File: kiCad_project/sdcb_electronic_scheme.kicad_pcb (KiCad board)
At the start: 2 copper layers, 144.8 x 99.1 mm, 70 parts, among them CON1 SD_Card, J1 POWER_12V, J10 BUTTON_RIGHT_TURN, J11 DB9, J2 Arduino_Nano_Header, J3 REAL_TIME_CLOCK, J4 LEFT_TURN_GYRO, J5 RIGHT_TURN_GYRO, J6 POWER_12V, J7 MOTOR, J8 BUTTON_ALL_DOWN_READ, J9 BUTTON_LEFT_TURN, Q1 BC817-40, Q2 BC817-40, U1 74HC595

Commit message: PCB v1
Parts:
- removed R18: 220 Ohm, Resistors_ThroughHole:Resistor_Horizontal_RM10mm
- added D16: D_Schottky, Diodes_ThroughHole:Diode_DO-41_SOD81_Horizontal_RM10, F.Cu at (71.1, 70.5)
- added D25: D_Schottky, Diodes_ThroughHole:Diode_DO-41_SOD81_Horizontal_RM10, F.Cu at (71.1, 64.1)
- added D26: D_Schottky, Diodes_ThroughHole:Diode_DO-41_SOD81_Horizontal_RM10, F.Cu at (71.1, 61.0)
- added D27: D_Schottky, Diodes_ThroughHole:Diode_DO-41_SOD81_Horizontal_RM10, F.Cu at (71.1, 57.8)
- added D28: D_Schottky, Diodes_ThroughHole:Diode_DO-41_SOD81_Horizontal_RM10, F.Cu at (72.4, 123.2)
- added D29: D_Schottky, Diodes_ThroughHole:Diode_DO-41_SOD81_Horizontal_RM10, F.Cu at (72.4, 119.4)
- added D30: D_Schottky, Diodes_ThroughHole:Diode_DO-41_SOD81_Horizontal_RM10, F.Cu at (72.4, 115.6)
- added D31: D_Schottky, Diodes_ThroughHole:Diode_DO-41_SOD81_Horizontal_RM10, F.Cu at (72.4, 111.8)
- added D32: D_Schottky, Diodes_ThroughHole:Diode_DO-41_SOD81_Horizontal_RM10, F.Cu at (72.4, 108.0)
- added D33: D_Schottky, Diodes_ThroughHole:Diode_DO-41_SOD81_Horizontal_RM10, F.Cu at (72.4, 100.3)
- added D34: D_Schottky, Diodes_ThroughHole:Diode_DO-41_SOD81_Horizontal_RM10, F.Cu at (256.5, -4.45)
- added D35: D_Schottky, Diodes_ThroughHole:Diode_DO-41_SOD81_Horizontal_RM10, F.Cu at (151.1, 161.3)
- added D36: D_Schottky, Diodes_ThroughHole:Diode_DO-41_SOD81_Horizontal_RM10, F.Cu at (240.7, -22.2)
- added J12: RELAY_CONTROL, Pin_Headers:Pin_Header_Straight_1x02, F.Cu at (388.6, 63.8)
- added J13: 220V, Connect:AK300-2, F.Cu at (160.0, 55.9)
- added J14: 30V MOTOR, Connect:AK300-2, F.Cu at (146.1, 55.9)
- added Q3: BC817-40, Housings_TO-92:TO-92_Molded_Wide_Oval, F.Cu at (330.7, 128.9)
- added RL3: FINDER-36.11.4001, sun_hold:sun_hold_scb1m1240, F.Cu at (236.9, -3.81)
- added U2: 74HC595, Housings_DIP:DIP-16_W7.62mm_LongPads, F.Cu at (87.6, 79.4)
- added U3: 74HC595, Housings_DIP:DIP-16_W7.62mm_LongPads, F.Cu at (87.6, 55.9)
- added U4: 74HC595, Housings_DIP:DIP-16_W7.62mm_LongPads, F.Cu at (87.6, 104.8)
- added U5: LTV-817, Housings_DIP:DIP-4_W7.62mm, F.Cu at (338.8, 116.3)
- added U6: LTV-817, Housings_DIP:DIP-4_W7.62mm_LongPads, F.Cu at (288.4, 121.9)
- added U7: LTV-817, Housings_DIP:DIP-4_W7.62mm_LongPads, F.Cu at (251.4, 148.6)
- added X1: Buzzer, Buzzer_Beeper_RevA_25Oct2010:MagneticBuzzer_ProSignal_ABT-410-RC_RevA_25Oct2010, F.Cu at (-21.0, 121.3)
- C2: value 2200 uF -> 2200uF 25V
- D10, D12, D14, D15, D8: value 5.1V 1.3W -> D_Schottky; footprint Discret:D3 -> Diodes_ThroughHole:Diode_DO-41_SOD81_Horizontal_RM10
- D17: value LED -> D_Schottky; footprint LEDs:LED-3MM -> Diodes_ThroughHole:Diode_DO-41_SOD81_Horizontal_RM10
- D2, D3, D4: value D -> 100V 2A
- J1, J7: footprint Pin_Headers:Pin_Header_Straight_2x01 -> Connect:AK300-2
- J10: value BUTTON_RIGHT_TURN -> B_RIGHT_T
- J11: footprint Connect:DB9MD -> Connect:DB9FC
- J6: value POWER_12V -> POWER_MOTOR; footprint Pin_Headers:Pin_Header_Straight_2x01 -> Connect:AK300-2
- J8: value BUTTON_ALL_DOWN_READ -> DB15; footprint Pin_Headers:Pin_Header_Straight_2x01 -> Connect:DB15FC
- J9: value BUTTON_LEFT_TURN -> B_LEFT_T
- Q1, Q2: footprint trans:TO-220_Bipolar-BCE_Vertical_LargePads -> Housings_TO-92:TO-92_Molded_Wide_Oval
- R11, R12, R16: value 100 Ohm -> 1k
- R13, R14, R15: value R -> 1k
- R19: value R -> 220Ohm
- R7, R8: value 1k -> 10k
- moved R5 306.4 mm to (385.4, 52.8), turned to 0 degrees
- moved R14 296.7 mm to (363.5, 88.0), turned to 0 degrees
- moved CON1 291.0 mm to (374.6, 195.6), turned to 0 degrees
- moved R13 279.5 mm to (348.5, 105.2), turned to 0 degrees
- moved R1 277.3 mm to (363.5, 78.6), turned to 0 degrees
- moved R6 268.3 mm to (351.0, 86.0), turned to 0 degrees
- moved R10 267.4 mm to (363.5, 69.2), turned to 0 degrees
- moved R4 251.2 mm to (336.0, 105.2), turned to 0 degrees
- moved Q2 243.8 mm to (386.6, 74.5), turned to 0 degrees
- moved R16 233.0 mm to (304.5, 149.4), turned to 0 degrees
- moved C3 226.4 mm to (299.4, 158.8), turned to 0 degrees
- moved R3 224.8 mm to (307.6, 128.6), turned to 0 degrees
- moved R15 220.9 mm to (292.0, 158.8), turned to 0 degrees
- moved Q1 215.9 mm to (361.1, 100.6), turned to 0 degrees
- moved J3 215.7 mm to (335.0, 54.4)
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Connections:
- D10 pad 2: GND -> Net-(D10-Pad2)
- D12 pad 2: GND -> Net-(D12-Pad2)
- D14 pad 2: GND -> Net-(D14-Pad2)
- D15 pad 2: GND -> Net-(D15-Pad2)
- D17 pad 1: GND -> Net-(D17-Pad1)
- D8 pad 2: GND -> Net-(D8-Pad2)
- F1 pad 1: +12V -> Net-(D3-Pad1)
- F1 pad 2: Net-(D3-Pad1) -> +12V
- J1 pad 1: Net-(D1-Pad1) -> Net-(D2-Pad1)
- J1 pad 2: Net-(D2-Pad1) -> Net-(D1-Pad1)
- J10 pad 1: Net-(J10-Pad1) -> Net-(D32-Pad1)
- J10 pad 2: GND -> Net-(J10-Pad2)
- J11 pad 2: Net-(J11-Pad2) -> Net-(D29-Pad1)
- J11 pad 3: Net-(J11-Pad3) -> Net-(D30-Pad1)
- J11 pad 4: Net-(J11-Pad4) -> Net-(D31-Pad1)
- J11 pad 6: GND -> Net-(J10-Pad2)
- J11 pad 7: GND -> Net-(J10-Pad2)
- J11 pad 8: GND -> Net-(J10-Pad2)
- J11 pad 9: GND -> Net-(J10-Pad2)
- J2 pad 16: Net-(D15-Pad1) -> Net-(J2-Pad16)
- J2 pad 19: Net-(D13-Pad1) -> Net-(J2-Pad19)
- J2 pad 27: +5V -> VCC
- J2 pad 5: Net-(D8-Pad1) -> Net-(J2-Pad5)
- J2 pad 6: Net-(D10-Pad1) -> Net-(J10-Pad2)
- J2 pad 7: Net-(D12-Pad1) -> Net-(C3-Pad2)
- J2 pad 8: Net-(D14-Pad1) -> Net-(J2-Pad8)
- J2 pad 9: Net-(C3-Pad2) -> Net-(J2-Pad9)
- J3 pad 4: +5V -> VCC
- J4 pad 1: +5V -> VCC
- J5 pad 1: +5V -> VCC
- J6 pad 1: Net-(F2-Pad2) -> Net-(F2-Pad1)
- J8 pad 1: Net-(J8-Pad1) -> Net-(D6-Pad1)
- J8 pad 2: Net-(J8-Pad2) -> Net-(D7-Pad1)
- J9 pad 1: Net-(J9-Pad1) -> Net-(D33-Pad1)
- J9 pad 2: GND -> Net-(J10-Pad2)
- Q1 pad 2: Net-(D6-Pad2) -> GND
- Q1 pad 3: GND -> Net-(D34-Pad2)
- Q2 pad 2: Net-(D7-Pad2) -> GND
- Q2 pad 3: GND -> Net-(D35-Pad2)
- R11 pad 1: Net-(J9-Pad1) -> Net-(R11-Pad1)
- R11 pad 2: Net-(D15-Pad1) -> GND
- R12 pad 1: Net-(J10-Pad1) -> VCC
- R12 pad 2: Net-(D13-Pad1) -> Net-(R12-Pad2)
- R13 pad 1: Net-(D8-Pad1) -> Net-(R13-Pad1)
- R13 pad 2: Net-(J11-Pad2) -> GND
- R14 pad 1: Net-(D10-Pad1) -> Net-(R14-Pad1)
- R14 pad 2: Net-(J11-Pad3) -> GND
- R15 pad 1: Net-(D12-Pad1) -> VCC
- R15 pad 2: Net-(J11-Pad4) -> Net-(R15-Pad2)
- R16 pad 1: Net-(D14-Pad1) -> VCC
- R16 pad 2: Net-(J11-Pad5) -> Net-(R16-Pad2)
- R7 pad 1: Net-(Q1-Pad1) -> Net-(R7-Pad1)
- R7 pad 2: Net-(J2-Pad1) -> GND
- R8 pad 1: Net-(J2-Pad2) -> Net-(R8-Pad1)
- R8 pad 2: Net-(Q2-Pad1) -> Net-(R8-Pad2)
- RL1 pad 12: Net-(Current1-Pad2) -> GND
- RL1 pad 14: Net-(F2-Pad1) -> Net-(F2-Pad2)
- RL1 pad A1: Net-(D6-Pad1) -> Net-(D34-Pad2)
- RL1 pad A2: Net-(Current1-Pad2) -> VCC
- RL2 pad 11: Net-(J7-Pad2) -> Net-(J14-Pad2)
- RL2 pad 14: Net-(F2-Pad1) -> Net-(J13-Pad1)
- RL2 pad A1: Net-(D7-Pad1) -> Net-(D35-Pad2)
- RL2 pad A2: GND -> VCC
- U1 pad 10: GND -> VCC
- U1 pad 11: Net-(J2-Pad10) -> Net-(J2-Pad8)
- U1 pad 13: +5V -> GND
- U1 pad 14: Net-(J2-Pad11) -> Net-(J2-Pad9)
- U1 pad 16: +5V -> VCC
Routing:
- net VCC: track 0.00 -> 94.0 mm
- net GND: track 0.00 -> 82.6 mm
- net Net-(D27-Pad1): track 0.00 -> 45.3 mm
- net Net-(D3-Pad1): track 0.00 -> 39.2 mm
- net Net-(D26-Pad1): track 0.00 -> 37.1 mm
- net Net-(D2-Pad1): track 0.00 -> 35.7 mm
- net +12V: track 0.00 -> 31.0 mm
- net Net-(D25-Pad1): track 0.00 -> 29.0 mm
- net Net-(R25-Pad1): track 0.00 -> 22.0 mm
- net Net-(D1-Pad1): track 0.00 -> 20.9 mm
- net Net-(D17-Pad1): track 0.00 -> 14.0 mm
- net Net-(D33-Pad2): track 0.00 -> 10.2 mm
- net Net-(R24-Pad1): track 0.00 -> 9.72 mm
- net Net-(U1-Pad7): track 0.00 -> 8.59 mm
- net Net-(D14-Pad2): track 0.00 -> 8.46 mm
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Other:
- net class Default: clearance 0.2 -> 0.4; trace_width 0.25 -> 0.5; via_dia 0.6 -> 1.5; via_drill 0.4 -> 0.7
- rule trace_clearance: 0.2 -> 0.4
- rule trace_min: 0.2 -> 0.5
- rule via_min_drill: 0.3 -> 0.7
- rule via_min_size: 0.4 -> 1.5

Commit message: PCB v2
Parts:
- added C4: 0.1 uF, Capacitors_ThroughHole:C_Disc_D6_P5, F.Cu at (98.0, 66.5)
- U6, U7: footprint Housings_DIP:DIP-4_W7.62mm_LongPads -> Housings_DIP:DIP-4_W7.62mm
- moved J7 272.9 mm to (402.0, 96.4), turned to 270 degrees
- moved RL2 252.7 mm to (377.7, 75.9), turned to 180 degrees
- moved J14 251.5 mm to (397.0, 72.4), turned to 90 degrees
- moved C3 239.5 mm to (60.3, 172.1), turned to 270 degrees
- moved J13 238.7 mm to (397.0, 84.1), turned to 90 degrees
- moved D35 237.5 mm to (371.9, 73.7), turned to 0 degrees
- moved RL1 221.6 mm to (382.9, 107.2), turned to 180 degrees
- moved D36 217.9 mm to (387.9, 138.4)
- moved RL3 202.0 mm to (382.9, 135.8)
- moved J6 200.7 mm to (363.5, 128.8), turned to 90 degrees
- moved R5 200.3 mm to (271.3, 217.4)
- moved R1 187.5 mm to (260.9, 235.5), turned to 270 degrees
- moved D34 163.2 mm to (377.7, 104.9)
- moved F2 157.2 mm to (359.9, 114.6)
- moved R6 147.3 mm to (284.5, 217.4)
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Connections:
- Current1 pad 1: GND -> Net-(Current1-Pad1)
- J6 pad 1: Net-(F2-Pad1) -> Net-(Current1-Pad2)
- J6 pad 2: GND -> Net-(F2-Pad1)
- R10 pad 2: GND -> Net-(Current1-Pad1)
- RL1 pad 12: GND -> Net-(Current1-Pad1)
- RL3 pad 12: Net-(Current1-Pad2) -> Net-(Current1-Pad1)
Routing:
- net GND: track 82.6 -> 158.2 mm
- net VCC: track 94.0 -> 153.0 mm
- net Net-(J7-Pad2): track 0.00 -> 53.8 mm
- net Net-(D35-Pad2): track 0.00 -> 38.1 mm
- net Net-(CON1-Pad5): track 0.00 -> 36.0 mm
- net Net-(D34-Pad2): track 0.00 -> 31.0 mm
- net Net-(F2-Pad2): track 0.00 -> 30.2 mm
- net Net-(Current1-Pad1): track 0.00 -> 29.2 mm
- net Net-(D36-Pad2): track 0.00 -> 26.1 mm
- net Net-(F2-Pad1): track 0.00 -> 20.6 mm
- net Net-(J7-Pad1): track 0.00 -> 20.5 mm
- net Net-(J13-Pad1): track 0.00 -> 19.9 mm
- net Net-(J14-Pad2): track 0.00 -> 19.8 mm
- net Net-(CON1-Pad2): track 0.00 -> 12.8 mm
- net Net-(Q2-Pad1): track 0.00 -> 11.5 mm
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
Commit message: 39 left39 left39 left
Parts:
- added 0R1: 0R, Resistors_ThroughHole:Resistor_Horizontal_RM10mm, F.Cu at (106.2, 86.9)
- added 0R2: 0R, Resistors_ThroughHole:Resistor_Horizontal_RM10mm, F.Cu at (103.6, 114.8)
- added 0R3: 0R, Resistors_ThroughHole:Resistor_Horizontal_RM10mm, F.Cu at (106.2, 111.5)
- added 0R4: 0R, Resistors_ThroughHole:Resistor_Horizontal_RM10mm, F.Cu at (100.6, 86.9)
- added R17: 0R, Resistors_ThroughHole:Resistor_Horizontal_RM15mm, F.Cu at (105.2, 101.1)
- CON1: footprint Connect:SD_Card_Receptacle -> Attend_SD_card_socket:SD_Attend
- Current1: footprint Resistors_ThroughHole:Resistor_Ceramic_Horizontal_L50mm-W14mm-H13mm-p60mm -> Resistor10W_vertical:Resistor_Horizontal_RM15mm
- D32, D33: footprint Diodes_ThroughHole:Diode_DO-41_SOD81_Horizontal_RM10 -> Diode_Smaller:Diode_DO-41_SOD81_Horizontal_RM10_SMALLER
- Q3: footprint Housings_TO-92:TO-92_Molded_Wide_Oval -> Housings_TO-92:TO-92_Inline_Wide
- R1: footprint Resistors_ThroughHole:Resistor_Horizontal_RM10mm -> Resistors_ThroughHole:Resistor_Horizontal_RM15mm
- R8: value 10k -> 1k
- RL2: footprint sun_hold:sun_hold_scb1m1240 -> sun_hold_ras0515:Relay_RAS-0515
- X1: footprint Buzzer_Beeper_RevA_25Oct2010:MagneticBuzzer_ProSignal_ABT-410-RC_RevA_25Oct2010 -> Buzzer_Beeper_RevA_25Oct2010:MagneticBuzzer_ProSignal_ABI-010-RC_RevA_25Oct2010
- moved J14 286.7 mm to (123.2, 157.4), turned to 0 degrees
- moved J13 283.5 mm to (123.2, 157.4), turned to 0 degrees
- moved RL2 276.9 mm to (113.7, 159.4), turned to 0 degrees
- moved D36 251.7 mm to (136.9, 118.9), turned to 90 degrees
- moved D35 250.0 mm to (122.2, 60.2), turned to 90 degrees
- moved D18 248.6 mm to (247.4, 68.6), turned to 270 degrees
- moved U6 245.9 mm to (111.5, 52.8)
- moved Q2 245.8 mm to (116.1, 53.1)
- moved R13 245.8 mm to (113.5, 50.0)
- moved R15 245.8 mm to (113.5, 63.8)
- moved R14 245.1 mm to (120.0, 110.5), turned to 270 degrees
- moved RL3 244.3 mm to (139.6, 113.9), turned to 270 degrees
- moved R16 243.8 mm to (123.2, 110.5), turned to 90 degrees
- moved D19 243.6 mm to (247.4, 74.7), turned to 270 degrees
- moved D20 239.1 mm to (247.4, 80.3), turned to 270 degrees
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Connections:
- C4 pad 1: Net-(C4-Pad1) -> Net-(0R2-Pad2)
- J2 pad 1: Net-(J2-Pad1) -> Net-(0R4-Pad1)
- J2 pad 16: Net-(J2-Pad16) -> Net-(C3-Pad2)
- J2 pad 2: Net-(J2-Pad2) -> Net-(0R2-Pad2)
- J2 pad 5: Net-(C4-Pad1) -> Net-(0R3-Pad2)
- J2 pad 6: Net-(J10-Pad2) -> Net-(D13-Pad1)
- J2 pad 7: Net-(C3-Pad2) -> Net-(J2-Pad7)
- R7 pad 1: Net-(R7-Pad1) -> Net-(R17-Pad1)
- R8 pad 1: Net-(R8-Pad1) -> Net-(R17-Pad1)
- R8 pad 2: Net-(R8-Pad2) -> Net-(D13-Pad1)
- U2 pad 11: Net-(J2-Pad10) -> Net-(0R4-Pad1)
- U2 pad 12: Net-(C4-Pad1) -> Net-(0R2-Pad2)
- U2 pad 14: Net-(J2-Pad11) -> Net-(U2-Pad14)
- U3 pad 11: Net-(J2-Pad10) -> Net-(0R4-Pad2)
- U3 pad 12: Net-(C4-Pad1) -> Net-(0R2-Pad2)
- U3 pad 14: Net-(U2-Pad9) -> Net-(0R1-Pad1)
- U3 pad 9: Net-(U3-Pad9) -> Net-(U2-Pad14)
- U4 pad 11: Net-(J2-Pad10) -> Net-(0R4-Pad1)
- U4 pad 12: Net-(C4-Pad1) -> Net-(0R2-Pad1)
- U4 pad 14: Net-(U3-Pad9) -> Net-(0R3-Pad1)
- U5 pad 1: Net-(J2-Pad2) -> Net-(J2-Pad11)
- U6 pad 1: Net-(J2-Pad16) -> Net-(J2-Pad7)
- U7 pad 1: Net-(J2-Pad1) -> Net-(J2-Pad10)
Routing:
- net Net-(CON1-Pad7): track 0.00 -> 97.7 mm
- net Net-(J10-Pad2): track 0.00 -> 89.2 mm
- net GND: track 158.2 -> 238.2 mm
- net Net-(0R2-Pad2): track 0.00 -> 79.7 mm
- net Net-(J2-Pad11): track 0.00 -> 78.4 mm
- net Net-(J2-Pad7): track 0.00 -> 53.7 mm
- net Net-(0R4-Pad1): track 0.00 -> 53.5 mm
- net +3V3: track 0.00 -> 44.5 mm
- net Net-(0R1-Pad2): track 0.00 -> 37.9 mm
- net Net-(J2-Pad24): track 0.00 -> 33.8 mm
- net Net-(J2-Pad23): track 0.00 -> 33.8 mm
- net Net-(0R1-Pad1): track 0.00 -> 29.6 mm
- net Net-(0R3-Pad2): track 0.00 -> 28.4 mm
- net Net-(J2-Pad12): track 0.00 -> 26.6 mm
- net Net-(CON1-Pad1): track 8.80 -> 34.5 mm
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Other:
- board text added: "pakeisti sd kortelę, pridėt RTC virš jos it pakeisti pinus pagal RTC ir gyro. ir tada tranzo kojas vienoj eilėj padaryti"

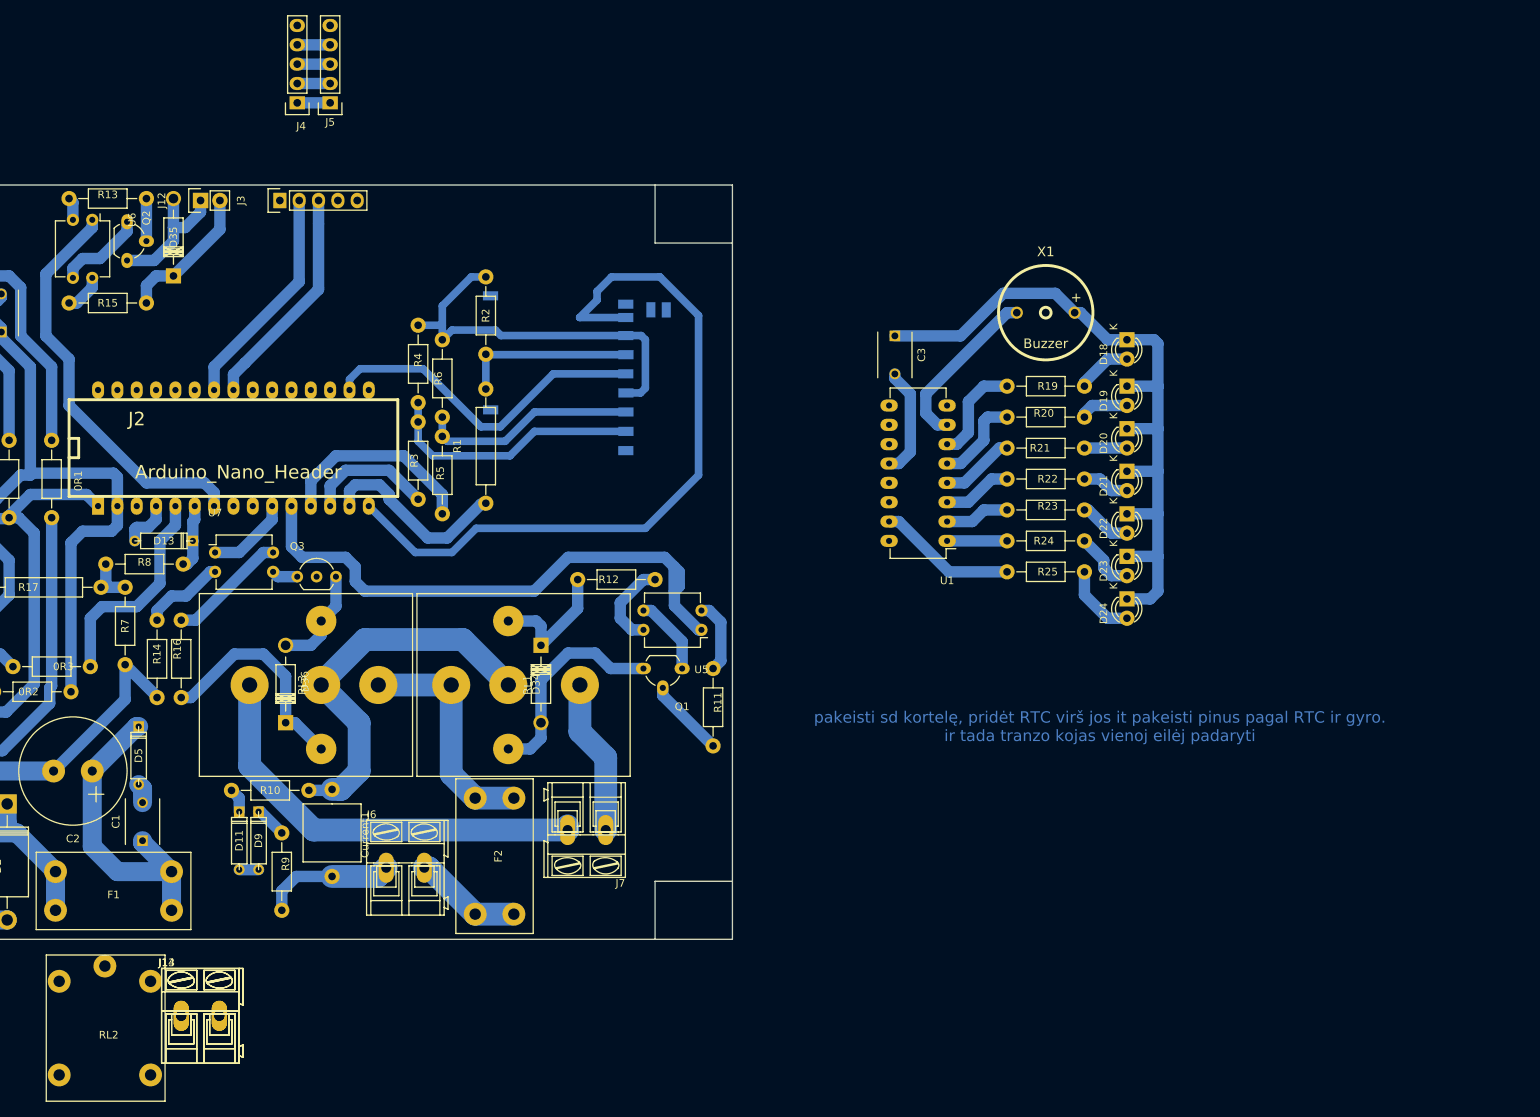
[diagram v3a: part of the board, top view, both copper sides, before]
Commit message: LEDs separated
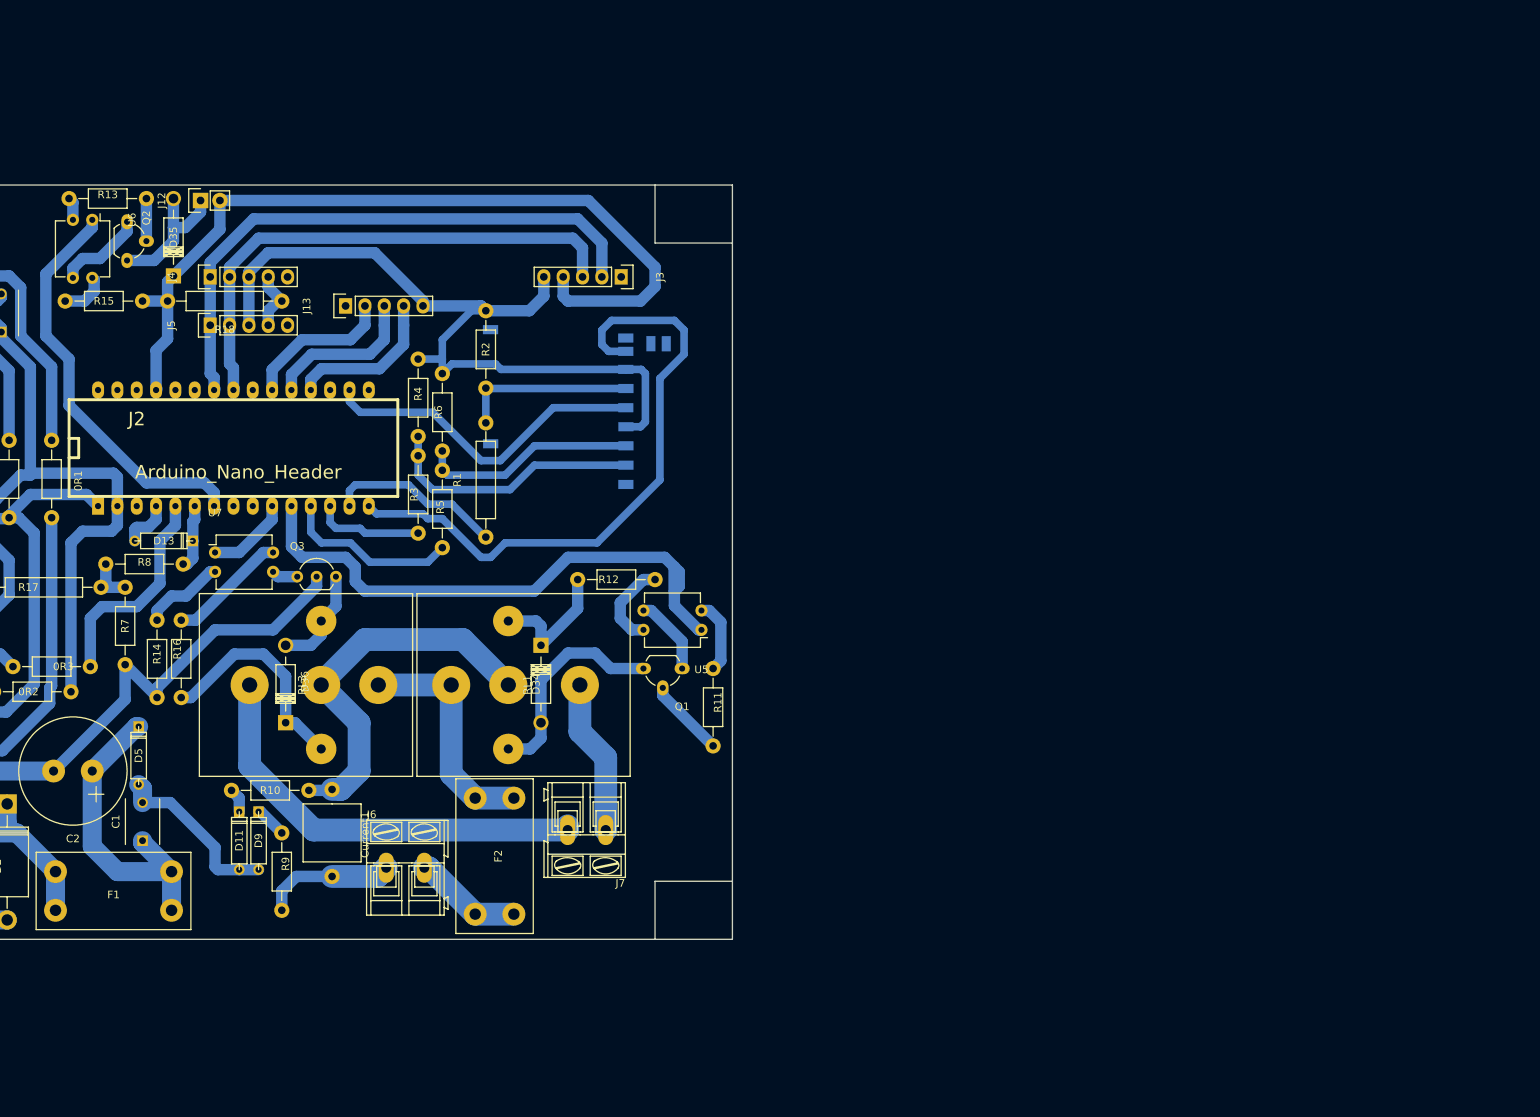
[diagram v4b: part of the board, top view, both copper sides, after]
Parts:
- removed C3: 0.1 uF, Capacitors_ThroughHole:C_Disc_D6_P5
- removed D18, D19, D20, D21, D22, D23, D24: LED, LEDs:LED-3MM
- removed J14: 30V MOTOR, Connect:AK300-2
- removed R19: 220Ohm, Resistors_ThroughHole:Resistor_Horizontal_RM10mm
- removed R20, R21, R22, R23, R24, R25: R, Resistors_ThroughHole:Resistor_Horizontal_RM10mm
- removed RL2: FINDER-36.11.4001, sun_hold_ras0515:Relay_RAS-0515
- removed U1: 74HC595, Housings_DIP:DIP-16_W7.62mm_LongPads
- removed X1: Buzzer, Buzzer_Beeper_RevA_25Oct2010:MagneticBuzzer_ProSignal_ABI-010-RC_RevA_25Oct2010
- added R18: 0R, Resistors_ThroughHole:Resistor_Horizontal_RM15mm, F.Cu at (128.9, 63.5)
- J13: value 220V -> HEADER_5; footprint Connect:AK300-2 -> Pin_Headers:Pin_Header_Straight_1x05
- moved J13 95.7 mm to (144.8, 64.1), turned to 90 degrees
- moved J3 45.9 mm to (181.0, 60.3), turned to 270 degrees
- moved J5 33.2 mm to (127.0, 66.7), turned to 90 degrees
- moved J4 25.6 mm to (127.0, 60.3), turned to 90 degrees
- moved CON1 4.45 mm to (179.8, 78.1)
- moved R1 4.45 mm to (163.2, 87.0)
- moved R3 4.45 mm to (154.3, 88.9)
- moved R4 4.45 mm to (154.3, 76.2)
- moved R5 4.45 mm to (157.5, 90.8)
- moved R6 4.45 mm to (157.5, 78.1)
- moved R2 4.44 mm to (163.2, 69.8)
- moved R15 0.57 mm to (113.0, 63.5)
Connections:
- J13 pad 1: Net-(J13-Pad1) -> VCC
- J2 pad 19: Net-(J2-Pad19) -> Net-(J13-Pad4)
- J2 pad 20: Net-(J2-Pad20) -> Net-(J13-Pad3)
- J2 pad 21: Net-(J2-Pad21) -> Net-(J13-Pad2)
- J4 pad 1: VCC -> Net-(J2-Pad24)
- J4 pad 2: GND -> Net-(J2-Pad23)
- J4 pad 3: Net-(J2-Pad24) -> GND
- J4 pad 4: Net-(J2-Pad23) -> Net-(J4-Pad4)
- J5 pad 1: VCC -> Net-(J2-Pad24)
- J5 pad 2: GND -> Net-(J2-Pad23)
- J5 pad 3: Net-(J2-Pad24) -> GND
- J5 pad 4: Net-(J2-Pad23) -> Net-(J4-Pad4)
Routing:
- net VCC: track 173.7 -> 261.4 mm
- net Net-(J2-Pad24): track 33.8 -> 76.7 mm
- net Net-(J2-Pad23): track 33.8 -> 68.8 mm
- net Net-(U1-Pad7): track 22.3 -> 0.00 mm
- net Net-(J13-Pad4): track 0.00 -> 20.6 mm
- net Net-(J13-Pad3): track 0.00 -> 20.6 mm
- net Net-(J13-Pad2): track 0.00 -> 19.8 mm
- net Net-(R25-Pad1): track 18.2 -> 0.00 mm
- net Net-(J2-Pad16): track 14.5 -> 0.00 mm
- net Net-(CON1-Pad7): track 97.7 -> 83.5 mm
- net Net-(R19-Pad1): track 13.4 -> 0.00 mm
- net Net-(R20-Pad1): track 11.9 -> 0.00 mm
- net Net-(D24-Pad2): track 9.90 -> 0.00 mm
- net Net-(R21-Pad1): track 9.77 -> 0.00 mm
- net Net-(R22-Pad1): track 9.14 -> 0.00 mm
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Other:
- board text removed: "pakeisti sd kortelę, pridėt RTC virš jos it pakeisti pinus pagal RTC ir gyro. ir tada tranzo kojas vienoj eilėj padaryti"
